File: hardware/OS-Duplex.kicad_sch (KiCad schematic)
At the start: 14 parts

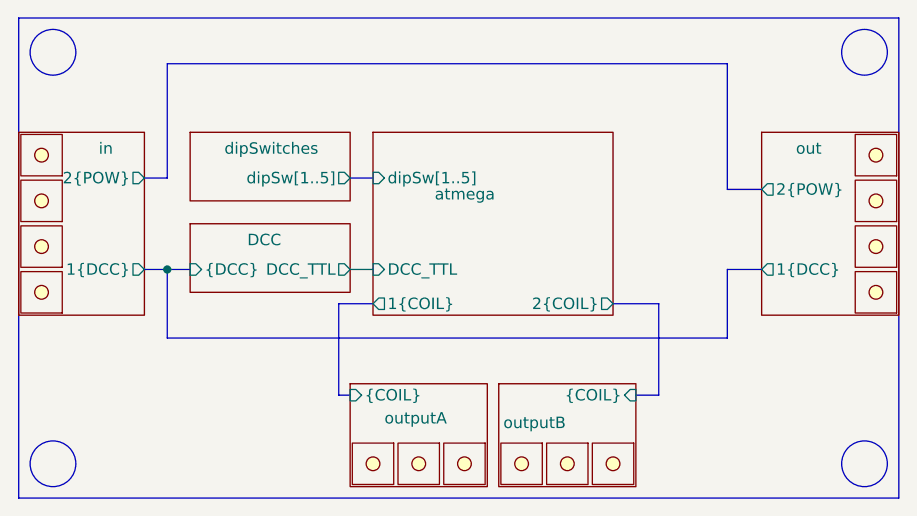
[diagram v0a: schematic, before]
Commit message: changed LDO
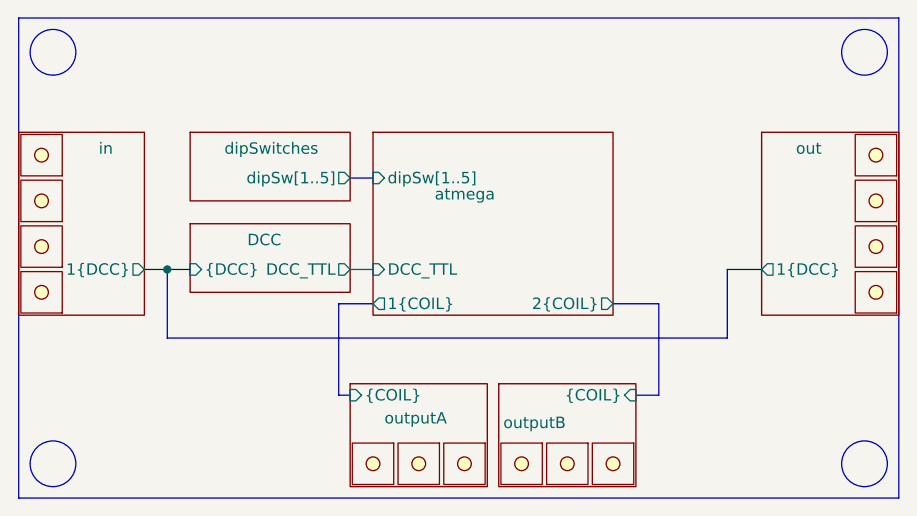
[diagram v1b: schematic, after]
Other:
- sheet in ports: added none; removed 2{POW}
- sheet out ports: added none; removed 2{POW}
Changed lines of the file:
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@@
-	(bus
-		(pts
-			(xy 69.85 113.03) (xy 69.85 100.33)
-		)
-		(stroke
-			(width 0)
-			(type default)
-		)
-	)
 	(bus
 		(pts
@@
 	(bus
 		(pts
-			(xy 67.31 113.03) (xy 69.85 113.03)
-		)
-		(stroke
-			(width 0)
-			(type default)
-		)
-	)
-	(bus
-		(pts
-			(xy 132.08 114.3) (xy 135.89 114.3)
-		)
-		(stroke
-			(width 0)
-			(type default)
-		)
-	)
-	(bus
-		(pts
 			(xy 132.08 130.81) (xy 132.08 123.19)
 		)
@@
 		(pts
 			(xy 90.17 113.03) (xy 92.71 113.03)
-		)
-		(stroke
-			(width 0)
-			(type default)
-		)
-	)
-	(bus
-		(pts
-			(xy 69.85 100.33) (xy 132.08 100.33)
-		)
-		(stroke
-			(width 0)
-			(type default)
-		)
-	)
-	(bus
-		(pts
-			(xy 132.08 100.33) (xy 132.08 114.3)
 		)
 		(stroke
@@
 			)
 		)
-		(pin "2{POW}" output
-			(at 135.89 114.3 180)
-			(effects
-				(font
-					(size 1.27 1.27)
-				)
-				(justify left)
-			)
-		)
-		(instances
-			(project "oneFit"
+		(instances
+			(project "OS-Duplex"
 				(path "/5298ac75-044e-4260-bbaf-3f2b608479b0"
 					(page "2")
@@
 		)
 		(instances
-			(project "oneFit"
+			(project "OS-Duplex"
 				(path "/5298ac75-044e-4260-bbaf-3f2b608479b0"
 					(page "4")
@@
 			)
 		)
-		(pin "2{POW}" output
-			(at 67.31 113.03 0)
-			(effects
-				(font
-					(size 1.27 1.27)
-				)
-				(justify right)
-			)
-		)
-		(instances
-			(project "oneFit"
+		(instances
+			(project "OS-Duplex"
 				(path "/5298ac75-044e-4260-bbaf-3f2b608479b0"
 					(page "3")
@@
 		)
 		(instances
-			(project "oneFit"
+			(project "OS-Duplex"
 				(path "/5298ac75-044e-4260-bbaf-3f2b608479b0"
 					(page "5")
@@
 		)
 		(instances
-			(project "oneFit"
+			(project "OS-Duplex"
 				(path "/5298ac75-044e-4260-bbaf-3f2b608479b0"
 					(page "8")
@@
 		)
 		(instances
-			(project "oneFit"
+			(project "OS-Duplex"
 				(path "/5298ac75-044e-4260-bbaf-3f2b608479b0"
 					(page "6")
@@
 		)
 		(instances
-			(project "oneFit"
+			(project "OS-Duplex"
 				(path "/5298ac75-044e-4260-bbaf-3f2b608479b0"
 					(page "10")

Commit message: added translations
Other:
- removed sheet out
- added sheet in1 (in1.kicad_sch)
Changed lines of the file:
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@@
 	(bus
 		(pts
-			(xy 69.85 130.81) (xy 132.08 130.81)
-		)
-		(stroke
-			(width 0)
-			(type default)
-		)
-	)
-	(bus
-		(pts
-			(xy 132.08 123.19) (xy 135.89 123.19)
-		)
-		(stroke
-			(width 0)
-			(type default)
-		)
-	)
-	(bus
-		(pts
-			(xy 69.85 123.19) (xy 69.85 130.81)
+			(xy 69.85 101.6) (xy 132.08 101.6)
+		)
+		(stroke
+			(width 0)
+			(type default)
+		)
+	)
+	(bus
+		(pts
+			(xy 132.08 123.19) (xy 137.16 123.19)
+		)
+		(stroke
+			(width 0)
+			(type default)
+		)
+	)
+	(bus
+		(pts
+			(xy 69.85 123.19) (xy 69.85 101.6)
 		)
 		(stroke
@@
 	(bus
 		(pts
-			(xy 132.08 130.81) (xy 132.08 123.19)
+			(xy 132.08 101.6) (xy 132.08 123.19)
 		)
 		(stroke
@@
 	)
 	(sheet
-		(at 135.89 107.95)
-		(size 15.24 20.32)
+		(at 137.16 107.95)
+		(size 13.97 20.32)
 		(stroke
 			(width 0.1524)
@@
 			(color 194 194 194 1.0000)
 		)
-		(property "Sheetname" "out"
-			(at 139.7 110.49 0)
+		(property "Sheetname" "in1"
+			(at 140.97 110.49 0)
 			(effects
 				(font
@@
 			)
 		)
-		(property "Sheetfile" "out.kicad_sch"
-			(at 135.89 128.8546 0)
+		(property "Sheetfile" "in1.kicad_sch"
+			(at 137.16 128.8546 0)
 			(effects
 				(font
@@
 		)
 		(pin "1{DCC}" output
-			(at 135.89 123.19 180)
+			(at 137.16 123.19 180)
 			(effects
 				(font
@@
 			(project "OS-Duplex"
 				(path "/5298ac75-044e-4260-bbaf-3f2b608479b0"
-					(page "2")
-				)
-			)
+					(page "7")
+				)
+			)
